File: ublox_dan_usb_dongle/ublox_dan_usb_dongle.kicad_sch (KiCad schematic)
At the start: 17 parts, among them J1 USB_A, J2 USB_A, J3 U.Fl, J4 EXT, U1 DAN-F10N, U2 CH340N, U4 USBLC6-2SC6, U5 MIC5365-3.3YC5

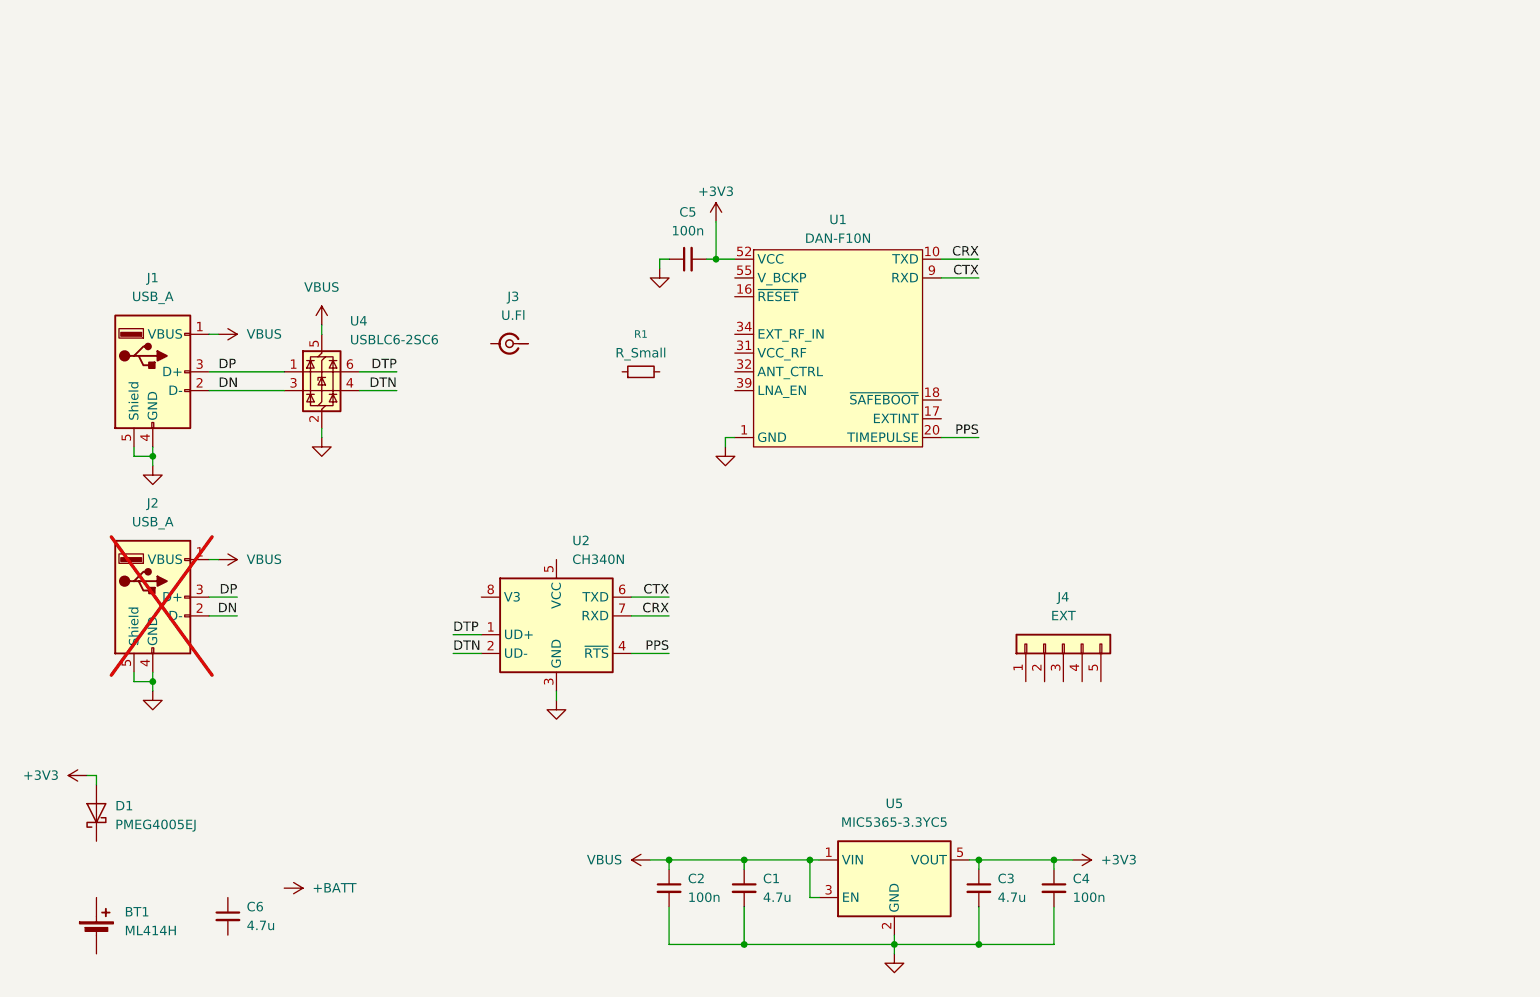
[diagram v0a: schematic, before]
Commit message: Update gitignore and finish USB GNSS dongle
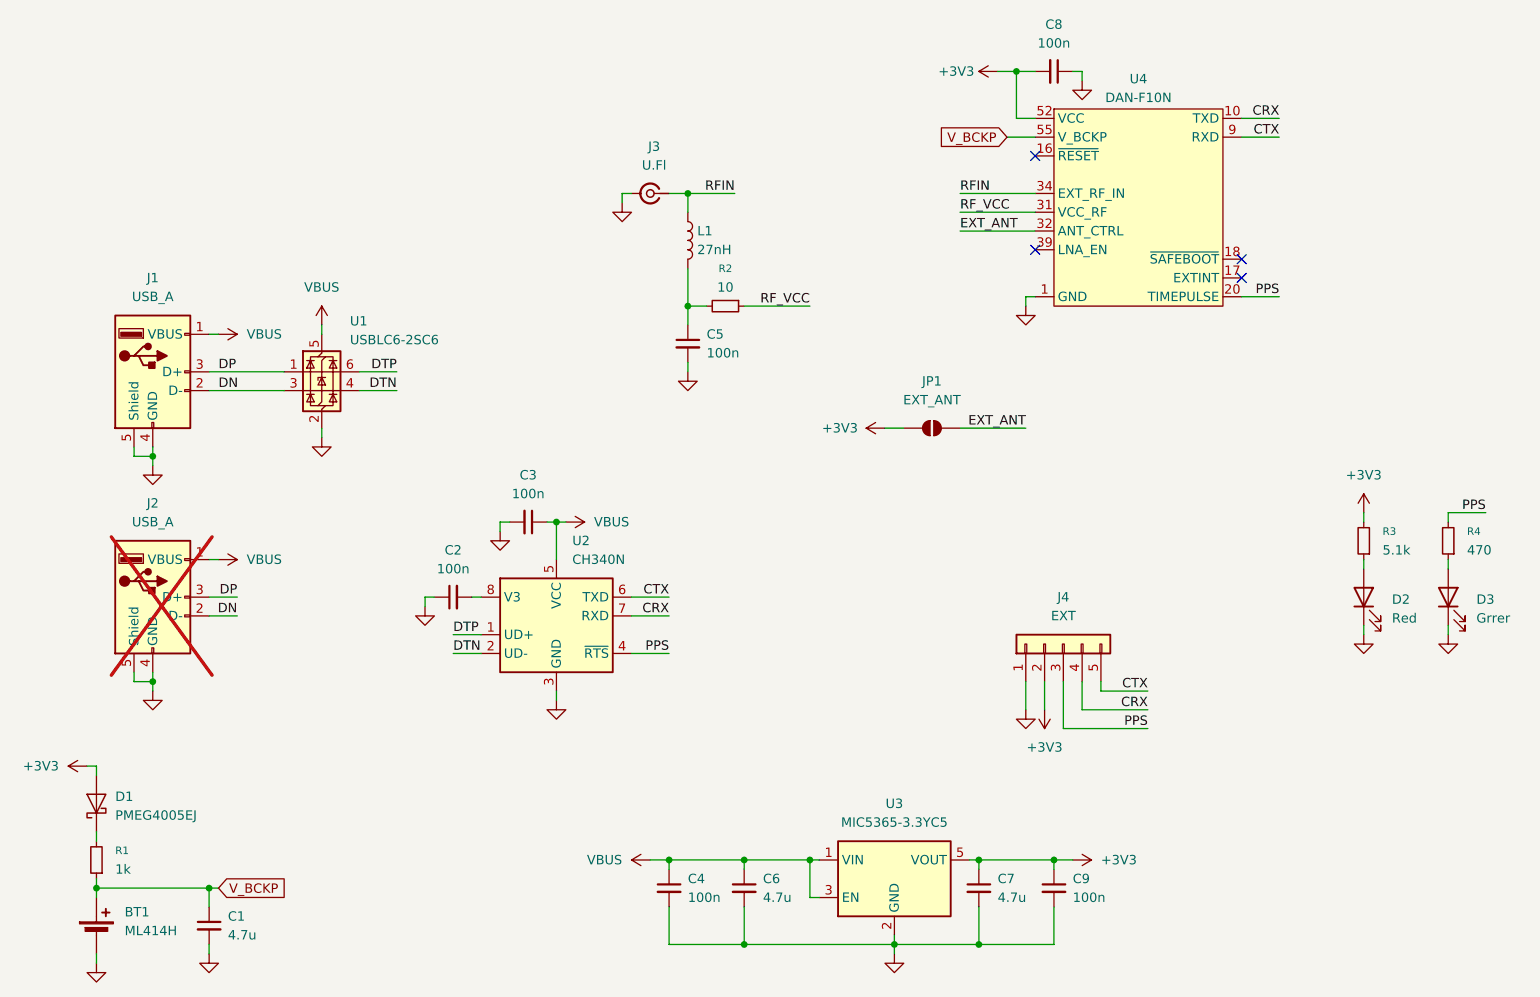
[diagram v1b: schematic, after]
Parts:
- added C2, C3, C5: 100n, Capacitor_SMD:C_0603_1608Metric_Pad1.08x0.95mm_HandSolder, symbol Device:C_Small
- added D2: Red, LED_SMD:LED_0805_2012Metric, symbol Device:LED
- added D3: Grrer, LED_SMD:LED_0805_2012Metric, symbol Device:LED
- added JP1: EXT_ANT, Jumper:SolderJumper-2_P1.3mm_Open_RoundedPad1.0x1.5mm, symbol Jumper:SolderJumper_2_Open
- added L1: 27nH, Inductor_SMD:L_0603_1608Metric, symbol Device:L
- added R2: 10, Resistor_SMD:R_0603_1608Metric_Pad0.98x0.95mm_HandSolder, symbol Device:R_Small
- added R3: 5.1k, Resistor_SMD:R_0603_1608Metric_Pad0.98x0.95mm_HandSolder, symbol Device:R_Small
- added R4: 470, Resistor_SMD:R_0603_1608Metric_Pad0.98x0.95mm_HandSolder, symbol Device:R_Small
- BT1: footprint (none) -> ML414H:ML414H_IV01E
- R1: value R_Small -> 1k
- renumbered C6 to C1, C2 to C4, C1 to C6, C3 to C7, C5 to C8, C4 to C9, U4 to U1, U5 to U3, U1 to U4
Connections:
- net +3V3: now also J4.2 (Pin_2), JP1.1 (A), R3.2
- net CRX: now also J4.4 (Pin_4)
- net CTX: now also J4.5 (Pin_5)
- net GND: now also BT1.2 (-), C1.2, J3.2 (Ext), J4.1 (Pin_1), C2.1, C3.2, C5.2, D2.1 (K), D3.1 (K)
- net PPS: now also J4.3 (Pin_3), R4.2
- net VBUS: now also U2.5 (VCC), C3.1
- net at D1.1 (K): now also R1.2
- net V_BCKP: now reaches C1.1
- net V_BCKP: now also BT1.1 (+), R1.1, U4.55 (V_BCKP)
- net at U2.8 (V3): now also C2.2
- net RFIN: now reaches J3.1 (In)
- net RFIN: now also U4.34 (EXT_RF_IN), L1.1
- net RF_VCC: now reaches U4.31 (VCC_RF)
- net RF_VCC: now also R2.1
- net EXT_ANT: now reaches U4.32 (ANT_CTRL)
- net EXT_ANT: now also JP1.2 (B)
- new net: D2.2 (A), R3.1
- new net: C5.1, L1.2, R2.2
- new net: D3.2 (A), R4.1
- no-connect marks 0 -> 4
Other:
- moved on the sheet: C1, C8, D1, J3, R1, U4
